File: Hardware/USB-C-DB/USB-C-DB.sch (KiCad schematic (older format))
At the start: 45 parts, among them J1 USB_C_Receptacle, J2 BatTP+, J3 JST Battery con, J4 BatTP-, U1 FT260S-U, U3 ESP-WROOM-02

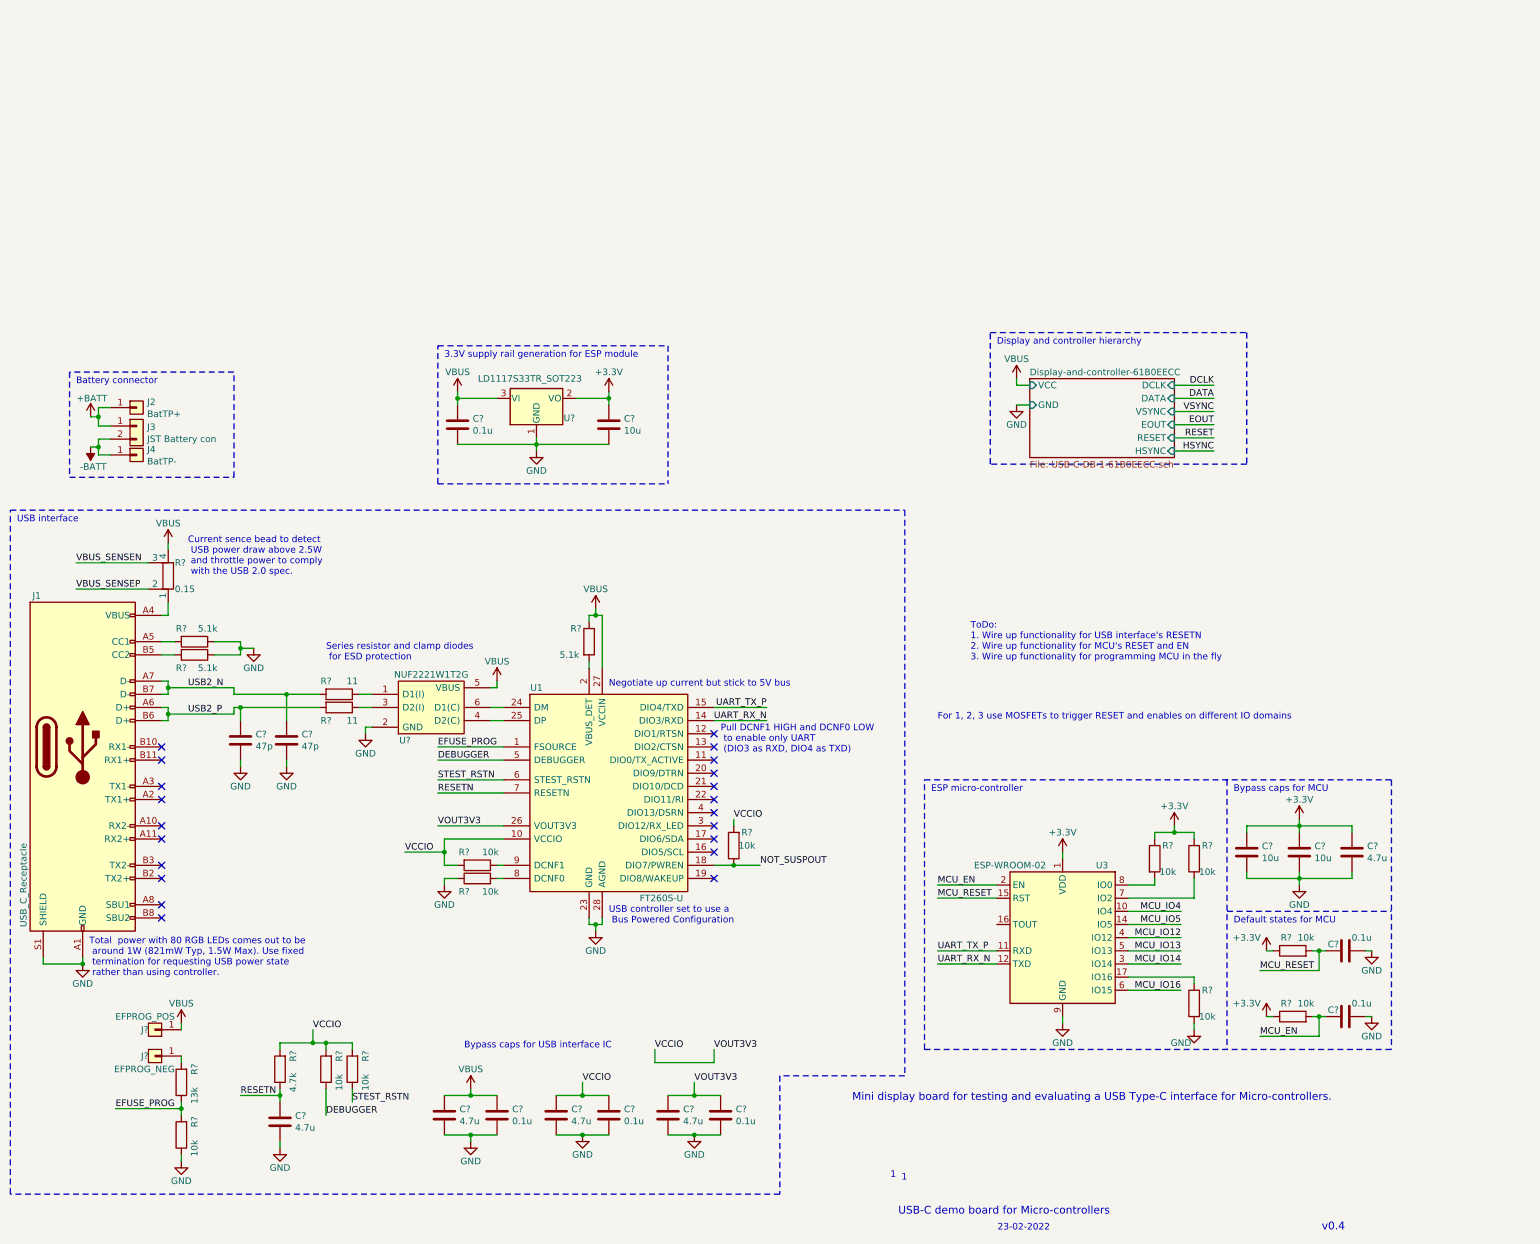
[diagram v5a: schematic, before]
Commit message: Adding auto program functionality
> Adding OSHW logo to schematics
> Adding Test points for select signals
> Updating README with schematic images
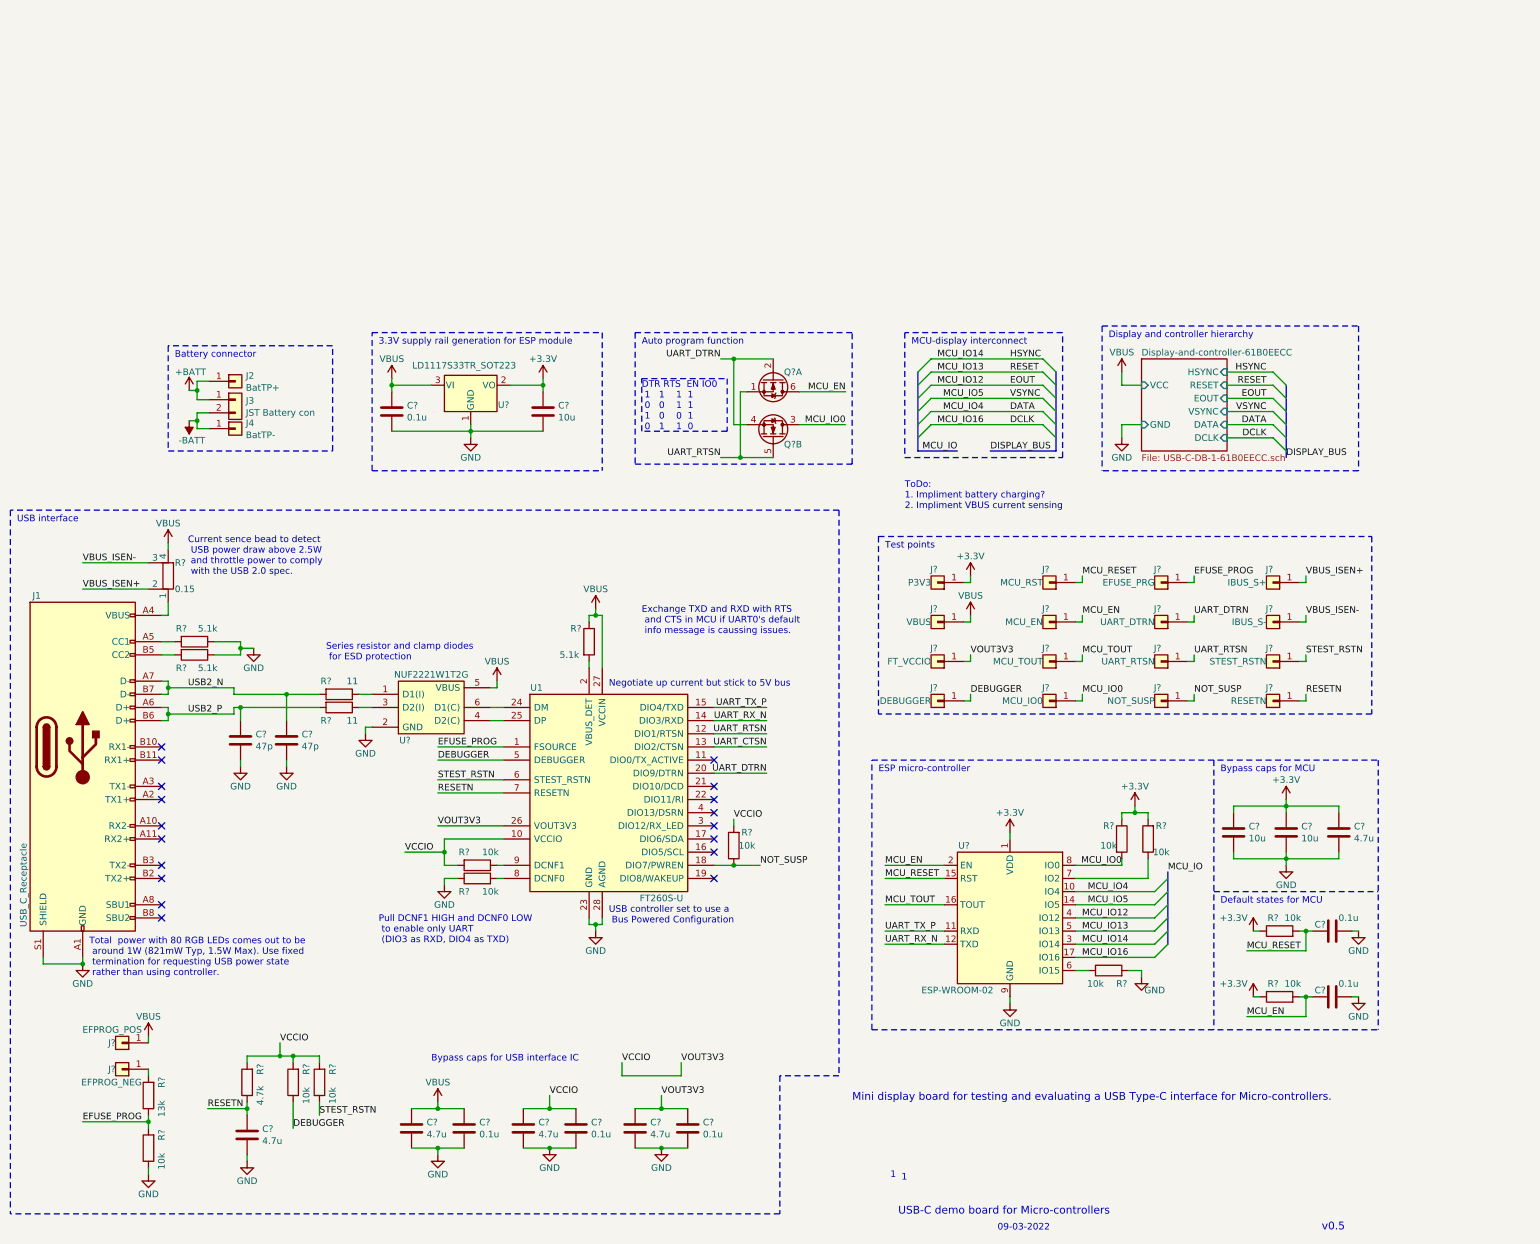
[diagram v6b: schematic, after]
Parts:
- removed U3: ESP-WROOM-02, RF_Module:ESP-WROOM-02, symbol RF_Module:ESP-WROOM-02
- added J?: P3V3, TestPoint:TestPoint_Pad_D4.0mm, symbol Connector_Generic:Conn_01x01
- added J?: MCU_RST, TestPoint:TestPoint_Pad_D4.0mm, symbol Connector_Generic:Conn_01x01
- added J?: MCU_EN, TestPoint:TestPoint_Pad_D4.0mm, symbol Connector_Generic:Conn_01x01
- added J?: VBUS, TestPoint:TestPoint_Pad_D4.0mm, symbol Connector_Generic:Conn_01x01
- added J?: EFUSE_PRG, TestPoint:TestPoint_Pad_D4.0mm, symbol Connector_Generic:Conn_01x01
- added J?: UART_DTRN, TestPoint:TestPoint_Pad_D4.0mm, symbol Connector_Generic:Conn_01x01
- added J?: FT_VCCIO, TestPoint:TestPoint_Pad_D4.0mm, symbol Connector_Generic:Conn_01x01
- added J?: UART_RTSN, TestPoint:TestPoint_Pad_D4.0mm, symbol Connector_Generic:Conn_01x01
- added J?: MCU_TOUT, TestPoint:TestPoint_Pad_D4.0mm, symbol Connector_Generic:Conn_01x01
- added J?: DEBUGGER, TestPoint:TestPoint_Pad_D4.0mm, symbol Connector_Generic:Conn_01x01
- added J?: MCU_IO0, TestPoint:TestPoint_Pad_D4.0mm, symbol Connector_Generic:Conn_01x01
- added J?: NOT_SUSP, TestPoint:TestPoint_Pad_D4.0mm, symbol Connector_Generic:Conn_01x01
- added J?: IBUS_S-, TestPoint:TestPoint_Pad_D4.0mm, symbol Connector_Generic:Conn_01x01
- added J?: IBUS_S+, TestPoint:TestPoint_Pad_D4.0mm, symbol Connector_Generic:Conn_01x01
- added J?: STEST_RSTN, TestPoint:TestPoint_Pad_D4.0mm, symbol Connector_Generic:Conn_01x01
- added J?: RESETN, TestPoint:TestPoint_Pad_D4.0mm, symbol Connector_Generic:Conn_01x01
- added Q? (x2): 2N7002KDW_R1_00001_seperate, SOT65P210X110-6N, symbol USB-C-DB-rescue:2N7002KDW_R1_00001_seperate
- added U?: ESP-WROOM-02, RF_Module:ESP-WROOM-02, symbol USB-C-DB-rescue:ESP-WROOM-02
- J2, J4, J? (x2): footprint TestPoint:TestPoint_Pad_4.0x4.0mm -> TestPoint:TestPoint_THTPad_D4.0mm_Drill2.0mm
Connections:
- net +3V3: now also J?.1 (Pin_1), U?.1 (VDD)
- net DATA: now also U?.10 (IO4)
- net DCLK: now also U?.17 (IO16)
- net DEBUGGER: now also J?.1 (Pin_1)
- net EFUSE_PROG: now also J?.1 (Pin_1)
- net EOUT: now also U?.4 (IO12)
- net GND: now also R?.2, U?.13 (GND), U?.18 (GND), U?.19 (GND), U?.9 (GND); no longer R?.1
- net HSYNC: now also U?.3 (IO14)
- net MCU_EN: now also J?.1 (Pin_1), Q?.6 (D1), U?.2 (EN)
- net MCU_IO13: now also U?.5 (IO13)
- net MCU_IO5: now also U?.14 (IO5)
- net MCU_RESET: now also J?.1 (Pin_1), U?.15 (RST)
- net RESETN: now also J?.1 (Pin_1)
- net STEST_RSTN: now also J?.1 (Pin_1)
- net UART_RX_N: now also U?.12 (TXD)
- net UART_TX_P: now also U?.11 (RXD)
- net VBUS: now also J?.1 (Pin_1)
- net VCCIO: now also J?.1 (Pin_1)
- net at R?.1: now also U?.7 (IO2)
- net MCU_IO0: now reaches R?.2
- net MCU_IO0: now also J?.1 (Pin_1), Q?.3 (D2), U?.8 (IO0)
- net UART_RTSN: now reaches U1.12 (DIO1/RTSN)
- net UART_RTSN: now also J?.1 (Pin_1), Q?.1 (S1), Q?.5 (G2)
- net UART_CTSN: now reaches U1.13 (DIO2/CTSN)
- net UART_DTRN: now reaches U1.20 (DIO9/DTRN)
- net UART_DTRN: now also J?.1 (Pin_1), Q?.2 (G1), Q?.4 (S2)
- net NOT_SUSPOUT renamed NOT_SUSP
- net NOT_SUSP: now also J?.1 (Pin_1)
- net VBUS_SENSEN renamed VBUS_ISEN-
- net VBUS_ISEN-: now also J?.1 (Pin_1)
- net VBUS_SENSEP renamed VBUS_ISEN+
- net VBUS_ISEN+: now also J?.1 (Pin_1)
- new net: R?.1, U?.6 (IO15)
- new net MCU_TOUT: J?.1 (Pin_1), U?.16 (TOUT)
- no-connect marks 21 -> 18
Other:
- note added: "09-03-2022"
- note added: "Auto program function"
- note added: "DTR RTS EN IO0\n 1 1 1 1\n 0 0 1 1\n 1 0 0 1\n 0 1 1 0"
- note added: "Exchange TXD and RXD with RTS\n and CTS in MCU if UART0's default\n info message is caussing issues."
- note added: "MCU-display interconnect"
- note added: "Test points"
- note added: "ToDo:\n1. Impliment battery charging?\n2. Impliment VBUS current sensing"
- note added: "v0.5"
- note removed: "23-02-2022"
- note removed: "For 1, 2, 3 use MOSFETs to trigger RESET and enables on different IO domains"
- note removed: "ToDo:\n1. Wire up functionality for USB interface's RESETN\n2. Wire up functionality for MCU's RESET and EN\n3. Wire up functionality for programming MCU in the fly"
- note removed: "v0.4"
- moved on the sheet: C?, J2, J3, J4, J?, R?, U?

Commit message: Cleaning up schematic after power budgeting
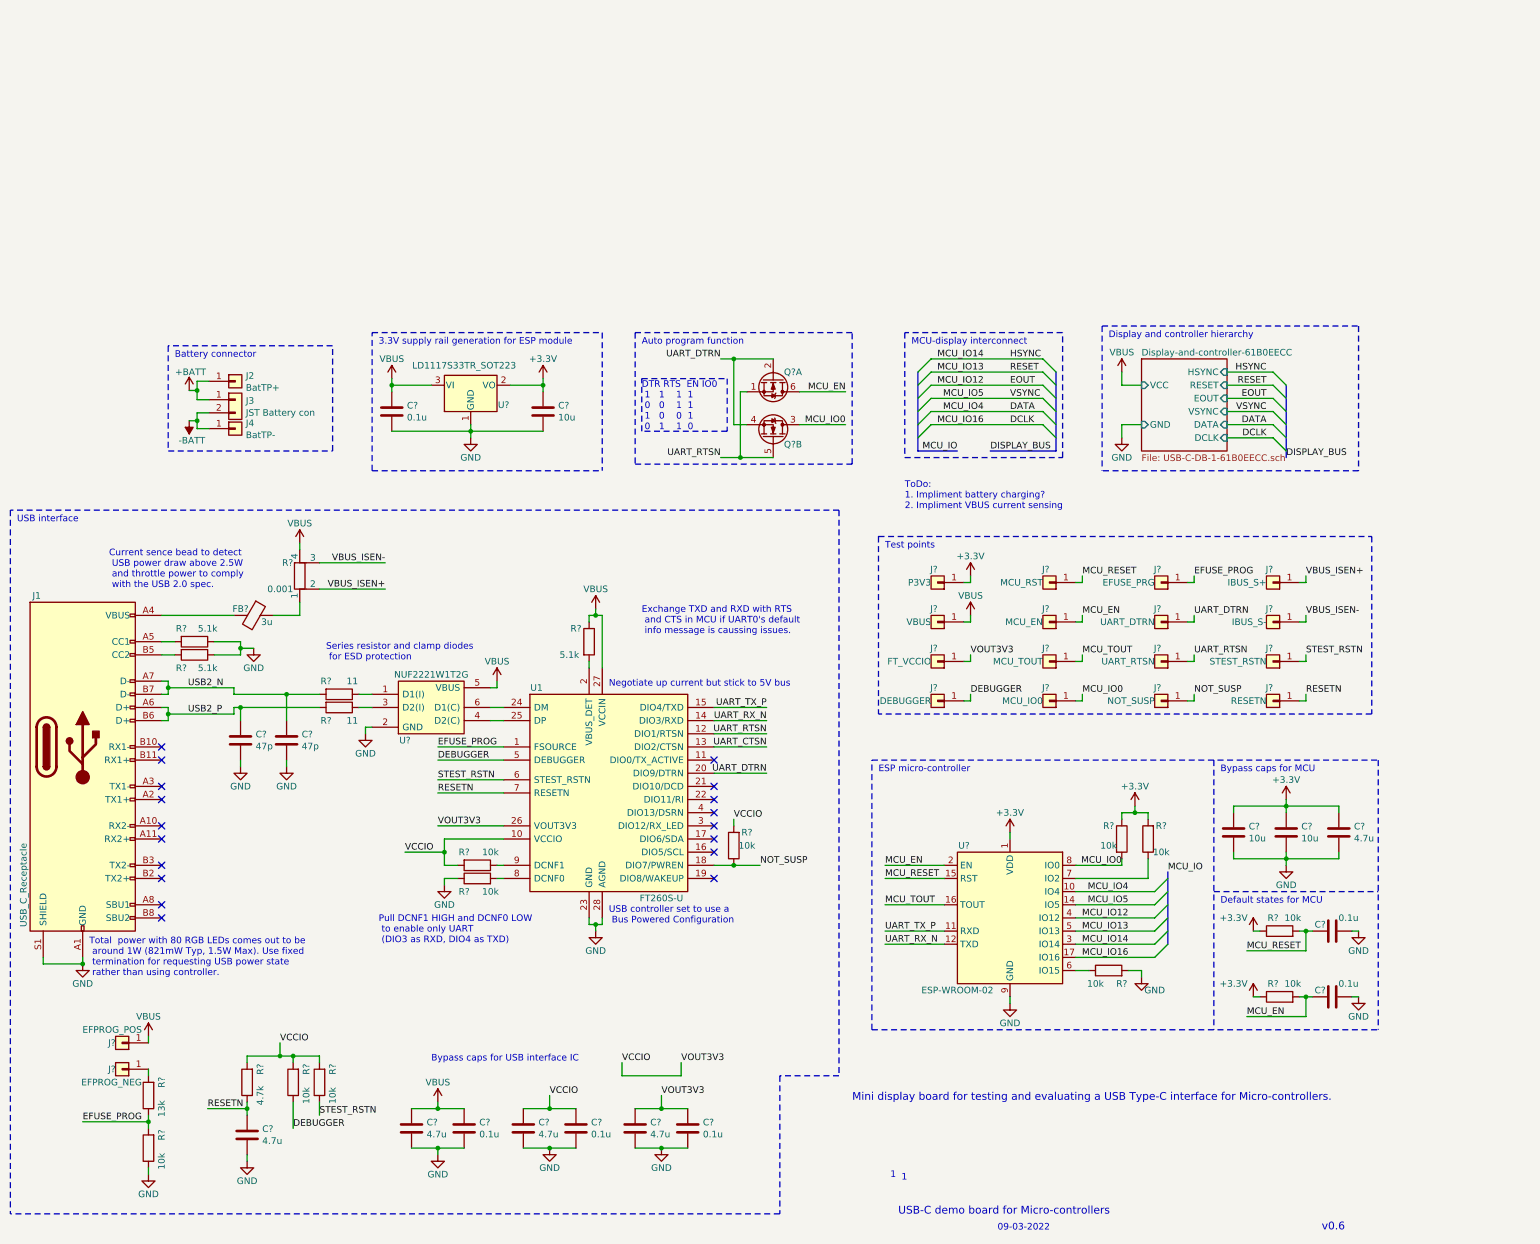
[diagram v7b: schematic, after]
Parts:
- removed R?: 0.15, Resistor_SMD:R_0603_1608Metric_Pad0.98x0.95mm_HandSolder, symbol Device:R_Shunt
- added FB?: 3u, Resistor_SMD:R_0603_1608Metric_Pad0.98x0.95mm_HandSolder, symbol Device:Ferrite_Bead
- added R?: 0.001, Resistor_SMD:R_0201_0603Metric_Pad0.64x0.40mm_HandSolder, symbol Device:R_Shunt
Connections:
- net VBUS: now also R?.4
- net VBUS_ISEN+: now also R?.2
- net VBUS_ISEN-: now also R?.3
- net at J1.A4 (VBUS), J1.A9 (VBUS), J1.B4 (VBUS)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: now also FB?.2
- new net: FB?.1, R?.1
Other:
- note added: "v0.6"
- note removed: "v0.5"
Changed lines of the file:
@@
 USB-C demo board for Micro-controllers
 Text Notes 10570 7635 0    59   ~ 0
-v0.5
+v0.6
 Text Notes 8105 7635 0    50   ~ 0
 09-03-2022
@@
 Text Notes 1200 5700 0    50   ~ 0
 Total  power with 80 RGB LEDs comes out to be\n around 1W (821mW Typ, 1.5W Max). Use fixed\n termination for requesting USB power state\n rather than using controller.
-Text Notes 1950 2650 0    50   ~ 0
+Text Notes 1350 2750 0    50   ~ 0
 Current sence bead to detect\n USB power draw above 2.5W\n and throttle power to comply\n with the USB 2.0 spec.
 $Comp
@@
 L power:VBUS #PWR?
 U 1 1 61B334E2
-P 1800 2400
-F 0 "#PWR?" H 1800 2250 50  0001 C CNN
-F 1 "VBUS" H 1800 2550 50  0000 C CNN
-F 2 "" H 1800 2400 50  0001 C CNN
-F 3 "" H 1800 2400 50  0001 C CNN
-	1    1800 2400
-	1    0    0    -1
+P 2800 2400
+F 0 "#PWR?" H 2800 2250 50  0001 C CNN
+F 1 "VBUS" H 2800 2550 50  0000 C CNN
+F 2 "" H 2800 2400 50  0001 C CNN
+F 3 "" H 2800 2400 50  0001 C CNN
+	1    2800 2400
+	-1   0    0    -1
 $EndComp
 $Comp
@@
 Wire Wire Line
 	1800 3500 2300 3500
-Wire Wire Line
-	1800 2950 1750 2950
 Text Notes 5150 3500 0    50   ~ 0
 Negotiate up current but stick to 5V bus
@@
 Wire Notes Line
 	8900 750  10850 750
-$Comp
-L Device:R_Shunt R?
-U 1 1 61D53208
-P 1800 2650
-F 0 "R?" H 1750 2550 50  0000 R CNN
-F 1 "0.15" H 1750 2750 50  0000 R CNN
-F 2 "Resistor_SMD:R_0603_1608Metric_Pad0.98x0.95mm_HandSolder" V 1730 2650 50  0001 C CNN
-F 3 "https://product.tdk.com/system/files/dam/doc/product/emc/emc/beads/catalog/beads_automotive_power_kpz1608-hr_en.pdf" H 1800 2650 50  0001 C CNN
-F 4 "KPZ1608SHR601ATD25" H 1800 2650 50  0001 C CNN "MPN"
-	1    1800 2650
-	-1   0    0    1
-$EndComp
-Wire Wire Line
-	1800 2850 1800 2950
 Wire Wire Line
-	1800 2400 1800 2450
-Text Label 1150 2750 0    50   ~ 0
+	2800 2400 2800 2450
+Text Label 3450 2750 2    50   ~ 0
 VBUS_ISEN+
-Text Label 1150 2550 0    50   ~ 0
+Text Label 3450 2550 2    50   ~ 0
 VBUS_ISEN-
 Text Label 6350 3750 2    50   ~ 0
@@
 	7000 800  5350 800
 Wire Wire Line
-	1150 2550 1650 2550
+	3450 2550 2950 2550
 Wire Wire Line
-	1650 2750 1150 2750
+	2950 2750 3450 2750
 Text Label 8200 1400 0    50   ~ 0
 DATA
@@
 	1    0    0    -1
 $EndComp
+Text Notes 7400 2150 0    50   ~ 0
+ToDo:\n1. Impliment battery charging?\n2. Impliment VBUS current sensing
+$Comp
+L Device:R_Shunt R?
+U 1 1 6285C594
+P 2800 2650
+F 0 "R?" H 2750 2550 50  0000 R CNN
+F 1 "0.001" H 2750 2750 50  0000 R CNN
+F 2 "Resistor_SMD:R_0201_0603Metric_Pad0.64x0.40mm_HandSolder" V 2730 2650 50  0001 C CNN
+F 3 "https://www.mouser.in/datasheet/2/447/PYu_RC_Group_51_RoHS_L_10-1664068.pdf" H 2800 2650 50  0001 C CNN
+F 4 "RC0201DR-071ML" H 2800 2650 50  0001 C CNN "MPN"
+	1    2800 2650
+	1    0    0    1
+$EndComp
+$Comp
+L Device:Ferrite_Bead FB?
+U 1 1 6285F074
+P 2450 2950
+F 0 "FB?" V 2400 2850 50  0000 C CNN
+F 1 "3u" V 2500 3050 50  0000 C CNN
+F 2 "Resistor_SMD:R_0603_1608Metric_Pad0.98x0.95mm_HandSolder" V 2380 2950 50  0001 C CNN
+F 3 "https://product.tdk.com/system/files/dam/doc/product/emc/emc/beads/catalog/beads_automotive_power_kpz1608-hr_en.pdf" H 2450 2950 50  0001 C CNN
+F 4 "KPZ1608SHR601ATD25" V 2450 2950 50  0001 C CNN "MPN"
+	1    2450 2950
+	0    1    1    0
+$EndComp
+Wire Wire Line
+	1750 2950 2300 2950
+Wire Wire Line
+	2600 2950 2800 2950
+Wire Wire Line
+	2800 2950 2800 2850
 Wire Bus Line
 	8550 1100 8550 1700
@@
 Wire Bus Line
 	9400 4900 9400 5450
-Text Notes 7400 2150 0    50   ~ 0
-ToDo:\n1. Impliment battery charging?\n2. Impliment VBUS current sensing
 $EndSCHEMATC
